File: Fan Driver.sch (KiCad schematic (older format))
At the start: 9 parts, among them Q2 MOSFET_N, Q3 MOSFET_N, Q4 MOSFET_N, U10 MCP4922-E/P, U2 OPA4170

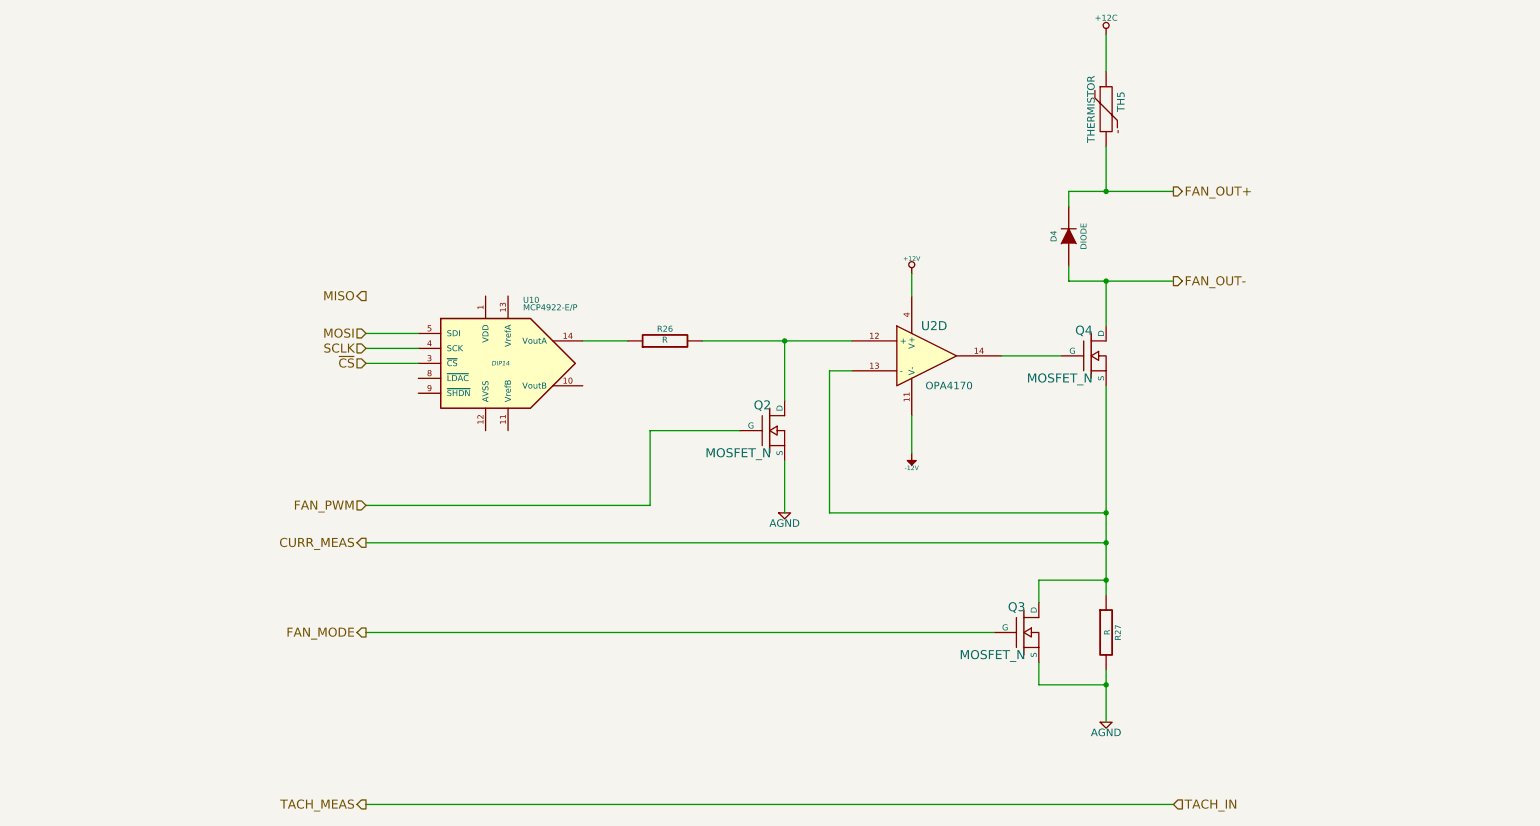
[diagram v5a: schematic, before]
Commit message: Initial layout of Arduino and Fan-Current
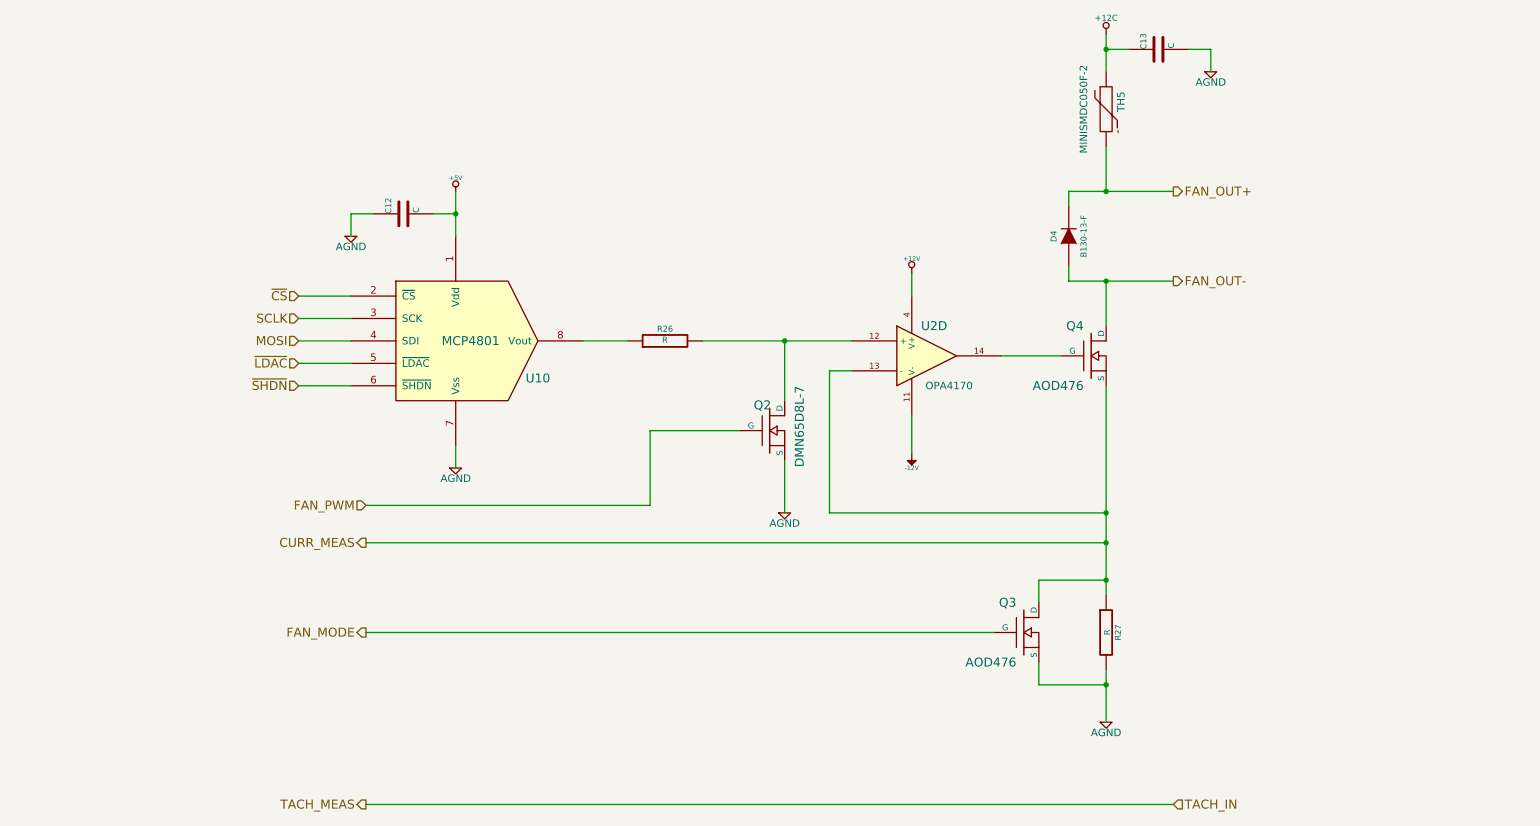
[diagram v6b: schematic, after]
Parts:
- removed Q3, Q4: MOSFET_N, ~, symbol MOSFET_N
- removed U10: MCP4922-E/P, DIP14, symbol MCP4922-E/P
- added C12, C13: C, ~, symbol C
- added Q3, Q4: AOD476, ~, symbol MOS_N_NUM
- added U10: MCP4801, symbol MCP4801
- D4: value DIODE -> B130-13-F; Distrib Part Num 1 (none) -> B130-FDICT; MFG Name (none) -> Diodes Inc.; MFG Part Num (none) -> B130-13-F
- Q2: value MOSFET_N -> DMN65D8L-7; Distrib Part Num 1 (none) -> DMN65D8L-7DICT; MFG Name (none) -> Diodes Inc.; MFG Part Num (none) -> DMN65D8L-7
- TH5: value THERMISTOR -> MINISMDC050F-2; Distrib Part Num 1 (none) -> MINISMDC050FCT; MFG Name (none) -> TE Connectivity; MFG Part Num (none) -> MINISMDC050F-2
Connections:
- net +12C: now also C13.1
- net AGND: now also C12.1, C13.2, Q3.3 (S), U10.7 (Vss)
- net CURR_MEAS: now also Q3.2 (D), Q4.3 (S)
- net FAN_MODE: now also Q3.1 (G)
- net FAN_OUT-: now also Q4.2 (D)
- net MOSI: now also U10.4 (SDI)
- net SCLK: now also U10.3 (SCK)
- net ~CS: now also U10.2 (~CS)
- net at U2.14: now also Q4.1 (G)
- net at R26.1: now also U10.8 (Vout)
- new net +5V: C12.2, U10.1 (Vdd)
- new net ~LDAC: U10.5 (~LDAC)
- new net ~SHDN: U10.6 (~SHDN)
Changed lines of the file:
@@
 $Descr A4 11693 8268
 encoding utf-8
-Sheet 7 9
+Sheet 9 9
 Title ""
-Date "21 feb 2014"
+Date "22 feb 2014"
 Rev ""
 Comp ""
@@
 $EndComp
 $Comp
-L MOSFET_N Q4
-U 1 1 52F27A2A
-P 7950 3500
-F 0 "Q4" H 7960 3670 60  0000 R CNN
-F 1 "MOSFET_N" H 7960 3350 60  0000 R CNN
-F 2 "~" H 7950 3500 60  0000 C CNN
-F 3 "~" H 7950 3500 60  0000 C CNN
-	1    7950 3500
-	1    0    0    -1
-$EndComp
-$Comp
 L R R27
 U 1 1 52F27A50
@@
 $EndComp
 $Comp
-L AGND #PWR048
+L AGND #PWR055
 U 1 1 52F27A5F
 P 8050 5950
-F 0 "#PWR048" H 8050 5950 40  0001 C CNN
+F 0 "#PWR055" H 8050 5950 40  0001 C CNN
 F 1 "AGND" H 8050 5880 50  0000 C CNN
 F 2 "" H 8050 5950 60  0000 C CNN
@@
 $EndComp
 $Comp
-L +12V #PWR049
+L +12V #PWR056
 U 1 1 52F27A88
 P 6750 2950
-F 0 "#PWR049" H 6750 2900 20  0001 C CNN
+F 0 "#PWR056" H 6750 2900 20  0001 C CNN
 F 1 "+12V" H 6750 3050 30  0000 C CNN
 F 2 "" H 6750 2950 60  0000 C CNN
@@
 $EndComp
 $Comp
-L -12V #PWR050
+L -12V #PWR057
 U 1 1 52F27A9B
 P 6750 4150
-F 0 "#PWR050" H 6750 4280 20  0001 C CNN
+F 0 "#PWR057" H 6750 4280 20  0001 C CNN
 F 1 "-12V" H 6750 4250 30  0000 C CNN
 F 2 "" H 6750 4150 60  0000 C CNN
@@
 $EndComp
 $Comp
-L AGND #PWR051
+L AGND #PWR058
 U 1 1 52F27AFD
 P 5900 4550
-F 0 "#PWR051" H 5900 4550 40  0001 C CNN
+F 0 "#PWR058" H 5900 4550 40  0001 C CNN
 F 1 "AGND" H 5900 4480 50  0000 C CNN
 F 2 "" H 5900 4550 60  0000 C CNN
 F 3 "" H 5900 4550 60  0000 C CNN
 	1    5900 4550
-	1    0    0    -1
-$EndComp
-$Comp
-L MCP4922-E/P U10
-U 1 1 52F27B2C
-P 4000 3550
-F 0 "U10" H 4150 3950 40  0000 L BNN
-F 1 "MCP4922-E/P" H 4150 3900 40  0000 L BNN
-F 2 "DIP14" H 4000 3550 30  0000 C CIN
-F 3 "" H 4000 3550 60  0000 C CNN
-	1    4000 3550
 	1    0    0    -1
 $EndComp
@@
 	0    -1   -1   0
 $EndComp
-Text HLabel 3100 3350 0    60   Input ~ 0
+Text HLabel 2650 3400 0    60   Input ~ 0
 MOSI
-Text HLabel 3100 3100 0    60   Output ~ 0
-MISO
-Text HLabel 3100 3550 0    60   Input ~ 0
+Text HLabel 2650 3100 0    60   Input ~ 0
 ~CS
-Text HLabel 3100 3450 0    60   Input ~ 0
+Text HLabel 2650 3250 0    60   Input ~ 0
 SCLK
-$Comp
-L MOSFET_N Q3
-U 1 1 52F3FFDA
-P 7500 5350
-F 0 "Q3" H 7510 5520 60  0000 R CNN
-F 1 "MOSFET_N" H 7510 5200 60  0000 R CNN
-F 2 "~" H 7500 5350 60  0000 C CNN
-F 3 "~" H 7500 5350 60  0000 C CNN
-	1    7500 5350
-	1    0    0    -1
-$EndComp
 $Comp
 L THERMISTOR TH5
@@
 P 8050 1850
 F 0 "TH5" V 8150 1900 50  0000 C CNN
-F 1 "THERMISTOR" V 7950 1850 50  0000 C CNN
+F 1 "MINISMDC050F-2" V 7900 1850 50  0000 C CNN
 F 2 "~" H 8050 1850 60  0000 C CNN
 F 3 "~" H 8050 1850 60  0000 C CNN
+F 4 "TE Connectivity" H 8050 1850 60  0001 C CNN "MFG Name"
+F 5 "MINISMDC050F-2" H 8050 1850 60  0001 C CNN "MFG Part Num"
+F 6 "MINISMDC050FCT" H 8050 1850 60  0001 C CNN "Distrib Part Num 1"
 	1    8050 1850
 	1    0    0    -1
@@
 P 7800 2700
 F 0 "D4" H 7800 2800 40  0000 C CNN
-F 1 "DIODE" H 7800 2600 40  0000 C CNN
+F 1 "B130-13-F" H 7800 2600 40  0000 C CNN
 F 2 "~" H 7800 2700 60  0000 C CNN
 F 3 "~" H 7800 2700 60  0000 C CNN
+F 4 "Diodes Inc." H 7800 2700 60  0001 C CNN "MFG Name"
+F 5 "B130-13-F" H 7800 2700 60  0001 C CNN "MFG Part Num"
+F 6 "B130-FDICT" H 7800 2700 60  0001 C CNN "Distrib Part Num 1"
 	1    7800 2700
 	0    -1   -1   0
@@
 	8050 4750 3100 4750
 Wire Wire Line
-	3100 3550 3450 3550
-Wire Wire Line
-	3450 3450 3100 3450
-Wire Wire Line
-	3100 3350 3450 3350
+	2650 3100 3000 3100
+Wire Wire Line
+	3000 3250 2650 3250
+Wire Wire Line
+	2650 3400 3000 3400
 Wire Wire Line
 	4550 3400 4850 3400
@@
 P 5800 4000
 F 0 "Q2" H 5810 4170 60  0000 R CNN
-F 1 "MOSFET_N" H 5810 3850 60  0000 R CNN
+F 1 "DMN65D8L-7" V 6000 4300 60  0000 R CNN
 F 2 "~" H 5800 4000 60  0000 C CNN
 F 3 "~" H 5800 4000 60  0000 C CNN
+F 4 "Diodes Inc." H 5800 4000 60  0001 C CNN "MFG Name"
+F 5 "DMN65D8L-7" H 5800 4000 60  0001 C CNN "MFG Part Num"
+F 6 "DMN65D8L-7DICT" H 5800 4000 60  0001 C CNN "Distrib Part Num 1"
 	1    5800 4000
 	1    0    0    -1
@@
 FAN_MODE
 $Comp
-L +12C #PWR052
+L +12C #PWR059
 U 1 1 52F40CFB
 P 8050 1350
-F 0 "#PWR052" H 8050 1320 30  0001 C CNN
+F 0 "#PWR059" H 8050 1320 30  0001 C CNN
 F 1 "+12C" H 8050 1460 40  0000 C CNN
 F 2 "" H 8050 1350 60  0000 C CNN
@@
 	1    0    0    -1
 $EndComp
+$Comp
+L MCP4801 U10
+U 1 1 530827D3
+P 3700 3400
+F 0 "U10" H 4250 3150 60  0000 C CNN
+F 1 "MCP4801" H 3800 3400 60  0000 C CNN
+F 2 "" H 3650 3750 60  0000 C CNN
+F 3 "" H 3650 3750 60  0000 C CNN
+F 4 "Microchip Technology" H 3700 3400 60  0001 C CNN "MFG Name"
+F 5 "MCP4801-E/SN" H 3700 3400 60  0001 C CNN "MFG Part Num"
+F 6 "MCP4801-E/SN" H 3700 3400 60  0001 C CNN "Distrib Part Num 1"
+	1    3700 3400
+	1    0    0    -1
+$EndComp
+Text HLabel 2650 3550 0    60   Input ~ 0
+~LDAC
+Text HLabel 2650 3700 0    60   Input ~ 0
+~SHDN
+Wire Wire Line
+	3000 3550 2650 3550
+Wire Wire Line
+	3000 3700 2650 3700
+$Comp
+L +5V #PWR060
+U 1 1 5308A242
+P 3700 2400
+F 0 "#PWR060" H 3700 2490 20  0001 C CNN
+F 1 "+5V" H 3700 2490 30  0000 C CNN
+F 2 "~" H 3700 2400 60  0000 C CNN
+F 3 "~" H 3700 2400 60  0000 C CNN
+	1    3700 2400
+	1    0    0    -1
+$EndComp
+Wire Wire Line
+	3700 2400 3700 2700
+$Comp
+L C C12
+U 1 1 5308A27B
+P 3350 2550
+F 0 "C12" H 3350 2650 40  0000 L CNN
+F 1 "C" H 3356 2465 40  0000 L CNN
+F 2 "~" H 3388 2400 30  0000 C CNN
+F 3 "~" H 3350 2550 60  0000 C CNN
+	1    3350 2550
+	0    -1   -1   0
+$EndComp
+$Comp
+L AGND #PWR061
+U 1 1 5308A28A
+P 3000 2700
+F 0 "#PWR061" H 3000 2700 40  0001 C CNN
+F 1 "AGND" H 3000 2630 50  0000 C CNN
+F 2 "~" H 3000 2700 60  0000 C CNN
+F 3 "~" H 3000 2700 60  0000 C CNN
+	1    3000 2700
+	1    0    0    -1
+$EndComp
+Wire Wire Line
+	3550 2550 3700 2550
+Connection ~ 3700 2550
+Wire Wire Line
+	3150 2550 3000 2550
+Wire Wire Line
+	3000 2550 3000 2700
+$Comp
+L AGND #PWR062
+U 1 1 5308A2EF
+P 3700 4250
+F 0 "#PWR062" H 3700 4250 40  0001 C CNN
+F 1 "AGND" H 3700 4180 50  0000 C CNN
+F 2 "~" H 3700 4250 60  0000 C CNN
+F 3 "~" H 3700 4250 60  0000 C CNN
+	1    3700 4250
+	1    0    0    -1
+$EndComp
+Wire Wire Line
+	3700 4100 3700 4250
+$Comp
+L C C13
+U 1 1 5308AF5A
+P 8400 1450
+F 0 "C13" H 8400 1550 40  0000 L CNN
+F 1 "C" H 8406 1365 40  0000 L CNN
+F 2 "~" H 8438 1300 30  0000 C CNN
+F 3 "~" H 8400 1450 60  0000 C CNN
+	1    8400 1450
+	0    -1   -1   0
+$EndComp
+Wire Wire Line
+	8200 1450 8050 1450
+Connection ~ 8050 1450
+$Comp
+L AGND #PWR063
+U 1 1 5308AFB7
+P 8750 1600
+F 0 "#PWR063" H 8750 1600 40  0001 C CNN
+F 1 "AGND" H 8750 1530 50  0000 C CNN
+F 2 "~" H 8750 1600 60  0000 C CNN
+F 3 "~" H 8750 1600 60  0000 C CNN
+	1    8750 1600
+	1    0    0    -1
+$EndComp
+Wire Wire Line
+	8750 1600 8750 1450
+Wire Wire Line
+	8750 1450 8600 1450
+$Comp
+L MOS_N_NUM Q4
+U 1 1 5308B4A8
+P 7950 3500
+F 0 "Q4" H 7900 3700 60  0000 R CNN
+F 1 "AOD476" H 7900 3300 60  0000 R CNN
+F 2 "~" H 7950 3500 60  0000 C CNN
+F 3 "~" H 7950 3500 60  0000 C CNN
+F 4 "Alpha and Omega" H 7950 3500 60  0001 C CNN "MFG Name"
+F 5 "AOD476" H 7950 3500 60  0001 C CNN "MFG Part Num"
+F 6 "785-1112-1" H 7950 3500 60  0001 C CNN "Distrib Part Num 1"
+	1    7950 3500
+	1    0    0    -1
+$EndComp
+$Comp
+L MOS_N_NUM Q3
+U 1 1 5308B4F2
+P 7500 5350
+F 0 "Q3" H 7450 5550 60  0000 R CNN
+F 1 "AOD476" H 7450 5150 60  0000 R CNN
+F 2 "~" H 7500 5350 60  0000 C CNN
+F 3 "~" H 7500 5350 60  0000 C CNN
+F 4 "Alpha and Omega" H 7500 5350 60  0001 C CNN "MFG Name"
+F 5 "AOD476" H 7500 5350 60  0001 C CNN "MFG Part Num"
+F 6 "785-1112-1" H 7500 5350 60  0001 C CNN "Distrib Part Num 1"
+	1    7500 5350
+	1    0    0    -1
+$EndComp

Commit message: Reorganization of power conditioning module
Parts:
- D4: Distrib Part Num 1 Link (none) -> http://www.digikey.com/product-detail/en/B130-13-F/B130-FDI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
- Q2: Distrib Part Num 1 Link (none) -> http://www.diodes.com/datasheets/DMN65D8L.pdf
- Q3, Q4: Distrib Part Num 1 Link (none) -> http://www.aosmd.com/res/data_sheets/AOD476.pdf
- TH5: Distrib Part Num 1 Link (none) -> http://documents.tycoelectronics.com/commerce/DocumentDeliv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
- U10: Distrib Part Num 1 Link (none) -> http://www.microchip.com/mymicrochip/filehandler.aspx?ddocn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
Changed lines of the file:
@@
 $EndComp
 $Comp
-L AGND #PWR055
+L AGND #PWR059
 U 1 1 52F27A5F
 P 8050 5950
-F 0 "#PWR055" H 8050 5950 40  0001 C CNN
+F 0 "#PWR059" H 8050 5950 40  0001 C CNN
 F 1 "AGND" H 8050 5880 50  0000 C CNN
 F 2 "" H 8050 5950 60  0000 C CNN
@@
 $EndComp
 $Comp
-L +12V #PWR056
+L +12V #PWR060
 U 1 1 52F27A88
 P 6750 2950
-F 0 "#PWR056" H 6750 2900 20  0001 C CNN
+F 0 "#PWR060" H 6750 2900 20  0001 C CNN
 F 1 "+12V" H 6750 3050 30  0000 C CNN
 F 2 "" H 6750 2950 60  0000 C CNN
@@
 $EndComp
 $Comp
-L -12V #PWR057
+L -12V #PWR061
 U 1 1 52F27A9B
 P 6750 4150
-F 0 "#PWR057" H 6750 4280 20  0001 C CNN
+F 0 "#PWR061" H 6750 4280 20  0001 C CNN
 F 1 "-12V" H 6750 4250 30  0000 C CNN
 F 2 "" H 6750 4150 60  0000 C CNN
@@
 $EndComp
 $Comp
-L AGND #PWR058
+L AGND #PWR062
 U 1 1 52F27AFD
 P 5900 4550
-F 0 "#PWR058" H 5900 4550 40  0001 C CNN
+F 0 "#PWR062" H 5900 4550 40  0001 C CNN
 F 1 "AGND" H 5900 4480 50  0000 C CNN
 F 2 "" H 5900 4550 60  0000 C CNN
@@
 F 5 "MINISMDC050F-2" H 8050 1850 60  0001 C CNN "MFG Part Num"
 F 6 "MINISMDC050FCT" H 8050 1850 60  0001 C CNN "Distrib Part Num 1"
+F 7 "http://documents.tycoelectronics.com/commerce/DocumentDelivery/DDEController?Action=showdoc&DocId=Specification+Or+Standard%7FSCD25063%7FH%7Fpdf%7FEnglish%7FENG_SS_SCD25063_H.pdf" H 8050 1850 60  0001 C CNN "Distrib Part Num 1 Link"
 	1    8050 1850
 	1    0    0    -1
@@
 F 5 "B130-13-F" H 7800 2700 60  0001 C CNN "MFG Part Num"
 F 6 "B130-FDICT" H 7800 2700 60  0001 C CNN "Distrib Part Num 1"
+F 7 "http://www.digikey.com/product-detail/en/B130-13-F/B130-FDICT-ND/815318" H 7800 2700 60  0001 C CNN "Distrib Part Num 1 Link"
 	1    7800 2700
 	0    -1   -1   0
@@
 F 5 "DMN65D8L-7" H 5800 4000 60  0001 C CNN "MFG Part Num"
 F 6 "DMN65D8L-7DICT" H 5800 4000 60  0001 C CNN "Distrib Part Num 1"
+F 7 "http://www.diodes.com/datasheets/DMN65D8L.pdf" H 5800 4000 60  0001 C CNN "Distrib Part Num 1 Link"
 	1    5800 4000
 	1    0    0    -1
@@
 FAN_MODE
 $Comp
-L +12C #PWR059
+L +12C #PWR063
 U 1 1 52F40CFB
 P 8050 1350
-F 0 "#PWR059" H 8050 1320 30  0001 C CNN
+F 0 "#PWR063" H 8050 1320 30  0001 C CNN
 F 1 "+12C" H 8050 1460 40  0000 C CNN
 F 2 "" H 8050 1350 60  0000 C CNN
@@
 F 5 "MCP4801-E/SN" H 3700 3400 60  0001 C CNN "MFG Part Num"
 F 6 "MCP4801-E/SN" H 3700 3400 60  0001 C CNN "Distrib Part Num 1"
+F 7 "http://www.microchip.com/mymicrochip/filehandler.aspx?ddocname=en547908" H 3700 3400 60  0001 C CNN "Distrib Part Num 1 Link"
 	1    3700 3400
 	1    0    0    -1
@@
 	3000 3700 2650 3700
 $Comp
-L +5V #PWR060
+L +5V #PWR064
 U 1 1 5308A242
 P 3700 2400
-F 0 "#PWR060" H 3700 2490 20  0001 C CNN
+F 0 "#PWR064" H 3700 2490 20  0001 C CNN
 F 1 "+5V" H 3700 2490 30  0000 C CNN
 F 2 "~" H 3700 2400 60  0000 C CNN
@@
 $EndComp
 $Comp
-L AGND #PWR061
+L AGND #PWR065
 U 1 1 5308A28A
 P 3000 2700
-F 0 "#PWR061" H 3000 2700 40  0001 C CNN
+F 0 "#PWR065" H 3000 2700 40  0001 C CNN
 F 1 "AGND" H 3000 2630 50  0000 C CNN
 F 2 "~" H 3000 2700 60  0000 C CNN
@@
 	3000 2550 3000 2700
 $Comp
-L AGND #PWR062
+L AGND #PWR066
 U 1 1 5308A2EF
 P 3700 4250
-F 0 "#PWR062" H 3700 4250 40  0001 C CNN
+F 0 "#PWR066" H 3700 4250 40  0001 C CNN
 F 1 "AGND" H 3700 4180 50  0000 C CNN
 F 2 "~" H 3700 4250 60  0000 C CNN
@@
 Connection ~ 8050 1450
 $Comp
-L AGND #PWR063
+L AGND #PWR067
 U 1 1 5308AFB7
 P 8750 1600
-F 0 "#PWR063" H 8750 1600 40  0001 C CNN
+F 0 "#PWR067" H 8750 1600 40  0001 C CNN
 F 1 "AGND" H 8750 1530 50  0000 C CNN
 F 2 "~" H 8750 1600 60  0000 C CNN
@@
 F 5 "AOD476" H 7950 3500 60  0001 C CNN "MFG Part Num"
 F 6 "785-1112-1" H 7950 3500 60  0001 C CNN "Distrib Part Num 1"
+F 7 "http://www.aosmd.com/res/data_sheets/AOD476.pdf" H 7950 3500 60  0001 C CNN "Distrib Part Num 1 Link"
 	1    7950 3500
 	1    0    0    -1
@@
 F 5 "AOD476" H 7500 5350 60  0001 C CNN "MFG Part Num"
 F 6 "785-1112-1" H 7500 5350 60  0001 C CNN "Distrib Part Num 1"
+F 7 "http://www.aosmd.com/res/data_sheets/AOD476.pdf" H 7500 5350 60  0001 C CNN "Distrib Part Num 1 Link"
 	1    7500 5350
 	1    0    0    -1
